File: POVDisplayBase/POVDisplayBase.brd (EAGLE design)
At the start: 80 x 99 mm, 35 parts, among them IC1 317EMP, IC2 STM32L052C8T, J1 FTSH-105, Q1 SSM3K329R, Q2 FQD10N20L, X1 MINI-USB-UX60-MB-5ST

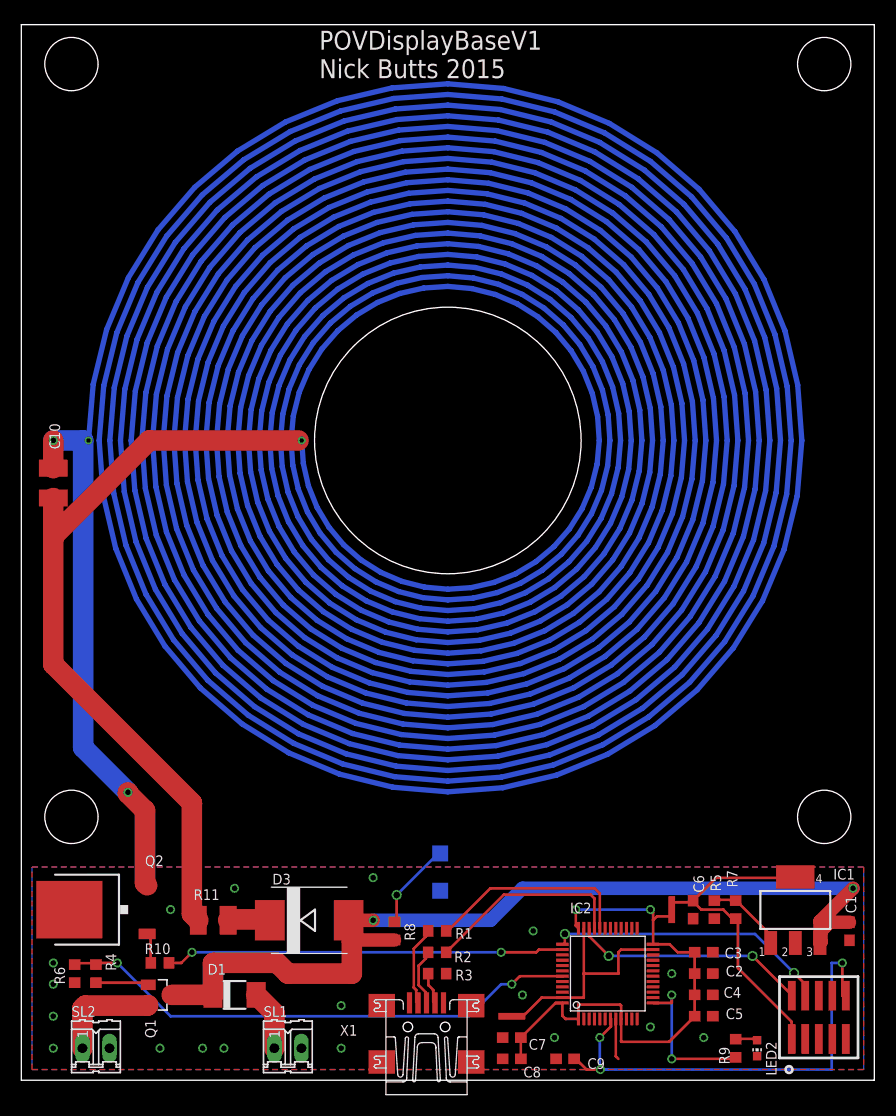
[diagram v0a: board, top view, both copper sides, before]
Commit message: Removed the processor and simplified the POVDisplayBase
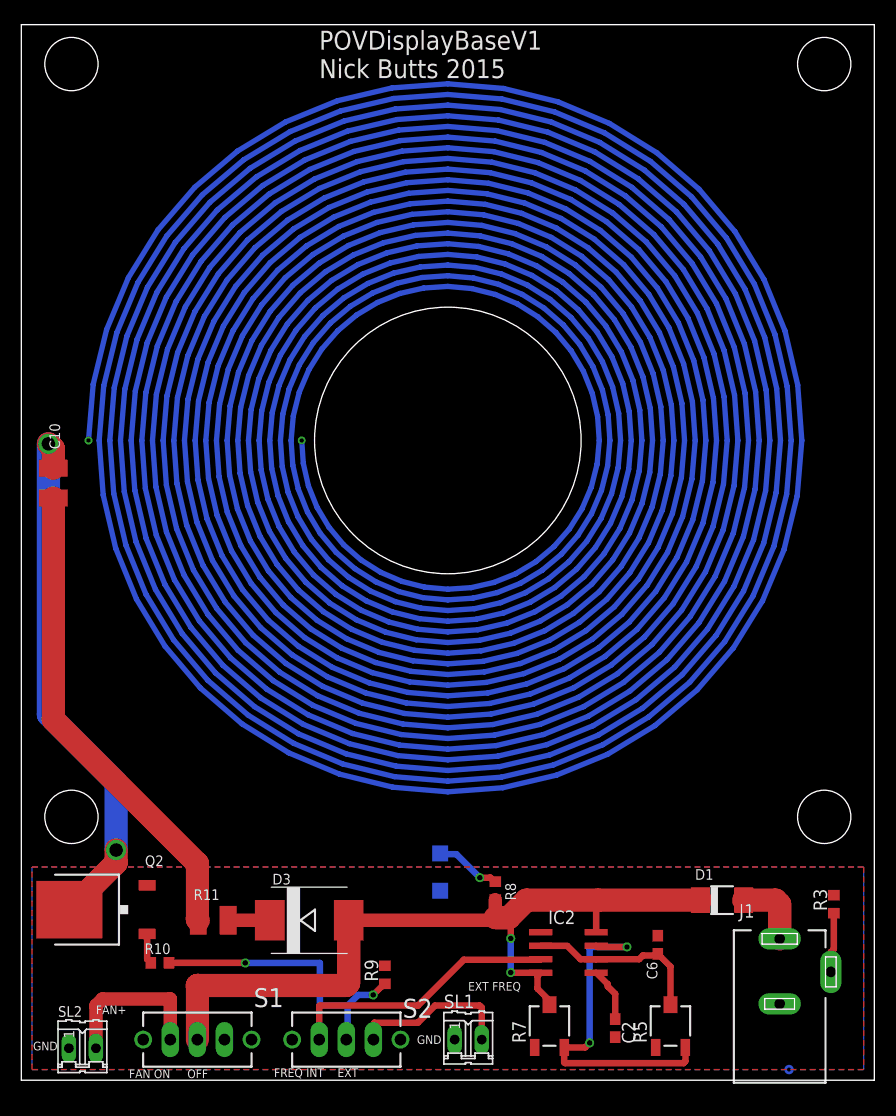
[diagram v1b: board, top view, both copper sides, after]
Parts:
- removed C1: 10u, resistor:C0603
- removed C3, C4, C9: 100n, resistor:C0603
- removed C5, C8: 1u, resistor:C0603
- removed C7: 10n, resistor:C0603
- removed IC1: 317EMP, linear:SOT223
- removed LED2: (no value), led:CHIP-LED0603
- removed Q1: SSM3K329R, NicksParts:SOT23
- removed R1, R2: 0, resistor:R0603
- removed R4: 10, resistor:R0603
- removed R6: 100k, resistor:R0603
- removed U$1, U$2: SHORT, NicksParts:SHORT
- removed X1: MINI-USB-UX60-MB-5ST, con-hirose:UX60-MB-5ST
- added S1, S2: TL36YO, switch:TL3XYO
- C2: value 100n -> DNP
- C6: value 10u -> 15p
- IC2: value STM32L052C8T -> NE555D; device micro-stm_v2:LQFP48 -> linear:SO08
- J1: value FTSH-105 -> DCJ0202; device NicksParts:FTSH-105-01-XXX-DV-K -> con-jack:DCJ0202
- R3: value 100k -> 0
- R5: value 200 -> 100; device resistor:R0603 -> pot:3223J
- R7: value 120 -> 100; device resistor:R0603 -> pot:3223J
- R9: value 180 -> 10K
- moved D1 46.6 mm to (65.7, 16.9)
- moved R3 37.8 mm to (76.2, 16.5), turned to 90 degrees
- moved R9 33.6 mm to (34.1, 9.89), turned to 90 degrees
- moved R7 20.6 mm to (49.5, 5.08)
- moved SL1 16.9 mm to (41.9, 3.81)
- moved R5 11.7 mm to (60.9, 5.08), turned to 90 degrees
- moved R8 10.2 mm to (44.5, 17.8)
- moved C2 9.76 mm to (55.7, 4.89), turned to 270 degrees
- moved J1 5.62 mm to (71.1, 10.2)
- moved C6 4.67 mm to (59.7, 12.7), turned to 90 degrees
- moved IC2 4.19 mm to (51.3, 12.0), turned to 270 degrees
- moved SL2 1.27 mm to (5.73, 3.00)
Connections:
- removed net +3V3: C6.1, IC1.4, J1.1, R7.1, U$2.P$2
- removed net DM: IC2.32, R1.1
- removed net DP: IC2.33, R2.1
- removed net FAN_EN: IC2.43, R4.2, R6.1
- removed net FAN_OUT: Q1.2, SL2.1
- removed net LED_RED: IC2.13, R9.2
- removed net N$10: Q1.1, R4.1
- removed net N$6: R3.2, X1.4
- removed net N$7: IC1.1, R5.1, R7.2
- removed net RESET: C9.1, IC2.7, J1.10
- removed net SWCLK: IC2.37, J1.4
- removed net SWDIO: IC2.34, J1.2
- removed net SWO: J1.6
- removed net UNPROTECTED_12V: D1.A, SL1.1
- removed net VDD: C2.1, C3.1, C4.1, C5.1, C7.1, C8.1, IC2.1, IC2.24, IC2.36, IC2.48, IC2.9, U$2.P$1
- removed net VSS: IC2.23, IC2.35, IC2.47, U$1.P$1
- new net CONNECTED: J1.2, R3.1
- new net N$13: S2.1, SL1.2
- new net N$14: C2.1, IC2.5
- new net N$3: S1.3, SL2.2
- new net NE555_OUT: IC2.3, S2.3
- net +12V: now also IC2.4, IC2.8, R7.2, S1.2; no longer C1.1, IC1.3, Q1.3
- net GND: now also IC2.1, Q2.2, R3.2, R9.2, SL1.1, SL2.1; no longer C1.2, C3.2, C4.2, C5.2, C7.2, C8.2, C9.2, IC2.44, IC2.8, J1.5, J1.9, LED2.C, Q2.3, R3.1, R5.2, R6.2, SL1.2, SL2.2, U$1.P$2, X1.5
- net N$4: now also D1.A, J1.1; no longer R2.2, X1.3
- net N$5: now also C6.1, IC2.2, IC2.6, R5.2; no longer R1.2, X1.2
- net N$9: now also IC2.7, R5.3, R7.3; no longer LED2.A, R9.1
- net NEG_COIL: now also Q2.3; no longer Q2.2
- net PWR_TRANSFER: now also R9.1, S2.2; no longer IC2.38
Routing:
- net VDD: track 51.0 -> 0.00 mm, vias 2 -> 0
- net FAN_EN: track 49.6 -> 0.00 mm, vias 2 -> 0
- net RESET: track 44.9 -> 0.00 mm, vias 3 -> 0
- net +3V3: track 30.9 -> 0.00 mm
- net N$9: track 2.05 -> 32.3 mm, vias 0 -> 2
- net SWCLK: track 26.7 -> 0.00 mm, vias 2 -> 0
- net POS_COIL: track 72.0 -> 45.2 mm
- net NE555_OUT: track 0.00 -> 25.7 mm
- net SWDIO: track 22.1 -> 0.00 mm, vias 2 -> 0
- net VSS: track 21.9 -> 0.00 mm
- net DM: track 19.5 -> 0.00 mm
- net DP: track 19.1 -> 0.00 mm
- net N$13: track 0.00 -> 15.5 mm
- net N$3: track 0.00 -> 15.0 mm
- net LED_RED: track 14.7 -> 0.00 mm, vias 2 -> 0
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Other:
- board text added: "EXT FREQ"
- board text added: "FAN ON OFF"
- board text added: "FAN+"
- board text added: "FREQ INT EXT"
- board text added: "GND"
